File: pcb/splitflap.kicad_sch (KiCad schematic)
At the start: 62 parts, among them J1 Motor A, J10 Hall C, J11 Hall-D, J12 Conn_01x03, J13 Conn_01x03, J14 Conn_01x03, J15 Conn_01x03, J2 Motor B, J3 Motor C, J4 Motor D, J6 Conn_01x03, J7 Barrel_Jack_Switch, J8 Hall A, J9 Hall B, SW1 A, SW2 B, SW3 IO0, SW4 RST, U1 ULN2003, U12 LM2596S-5, U2 ULN2003, U3 ESP32-DevKitC, U4 ULN2003, U5 AH1815-W-7, U6 AH1815-W-7, U7 AH1815-W-7, U8 AH1815-W-7, U9 AH1815-W-7

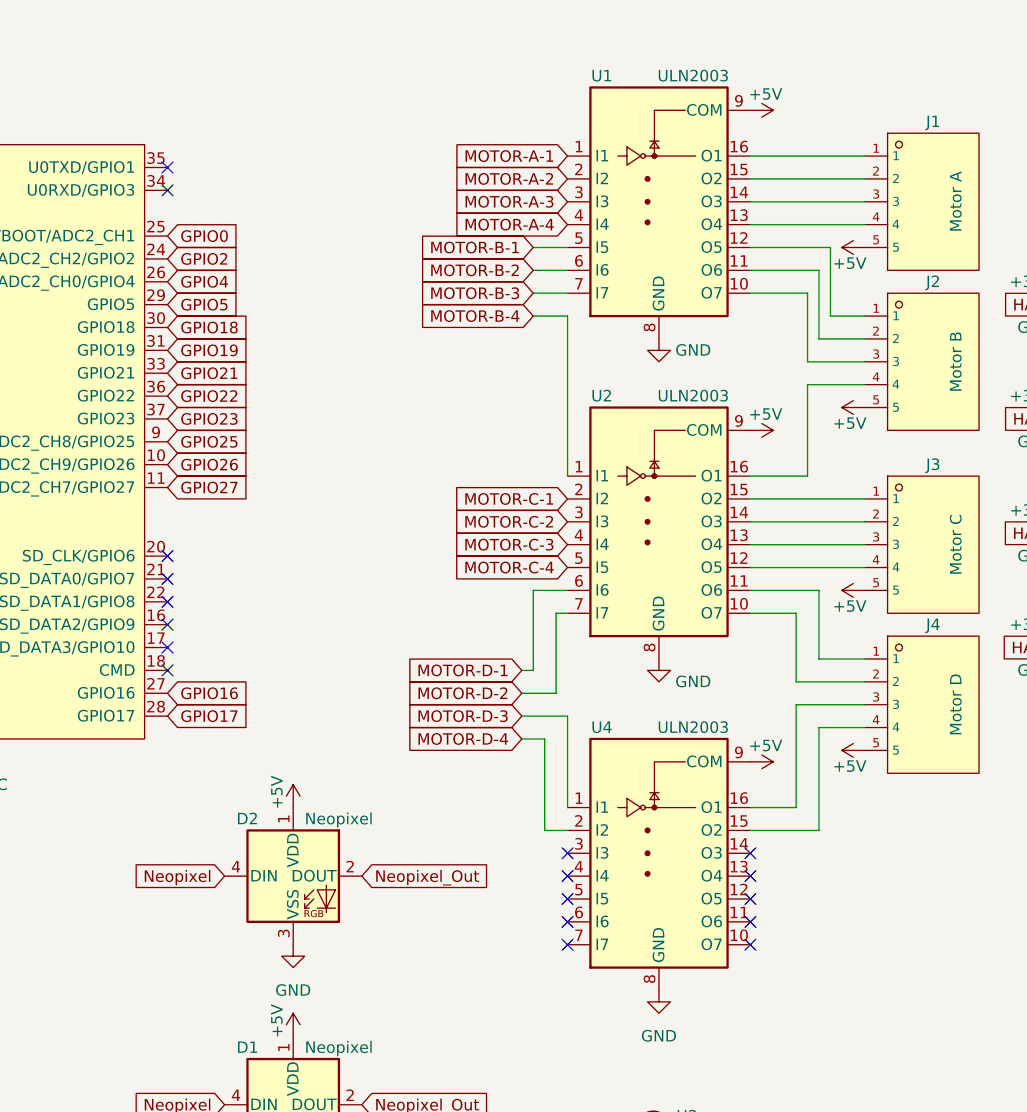
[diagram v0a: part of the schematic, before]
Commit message: Rework 1
Per EE.SO answer https://electronics.stackexchange.com/a/740530/10810
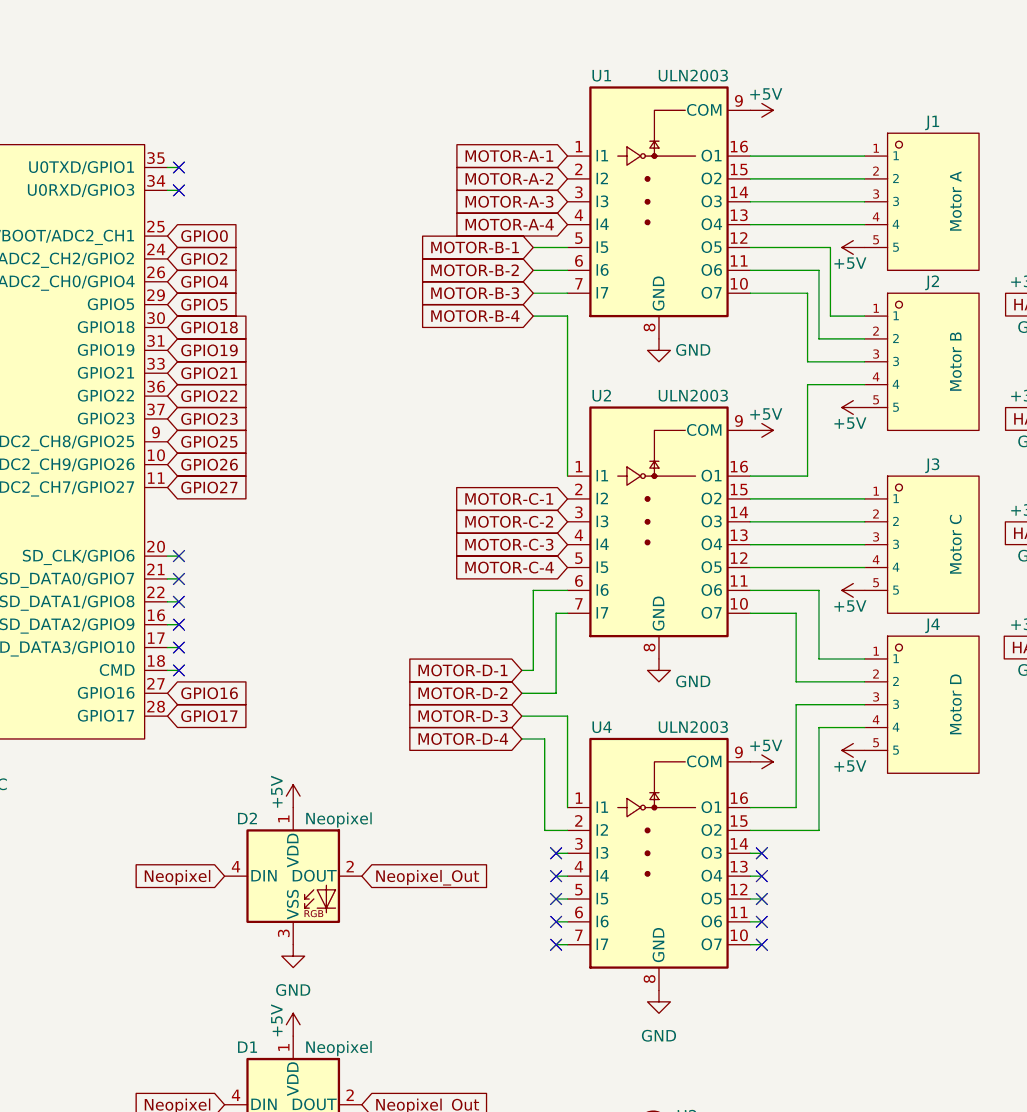
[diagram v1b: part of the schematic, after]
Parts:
- D3: footprint Diode_THT:D_DO-201_P12.70mm_Horizontal -> Diode_THT:D_DO-201_P15.24mm_Horizontal
- TP3: Label1 (none) -> SDA; Label2 (none) -> IO12
- TP4: Label1 (none) -> SCL; Label2 (none) -> IO14
- U1, U2, U4: footprint jlc_footprints:SOIC-16_L9.9-W3.9-P1.27-LS6.0-BL -> Package_SO:SOIC-16_3.9x9.9mm_P1.27mm

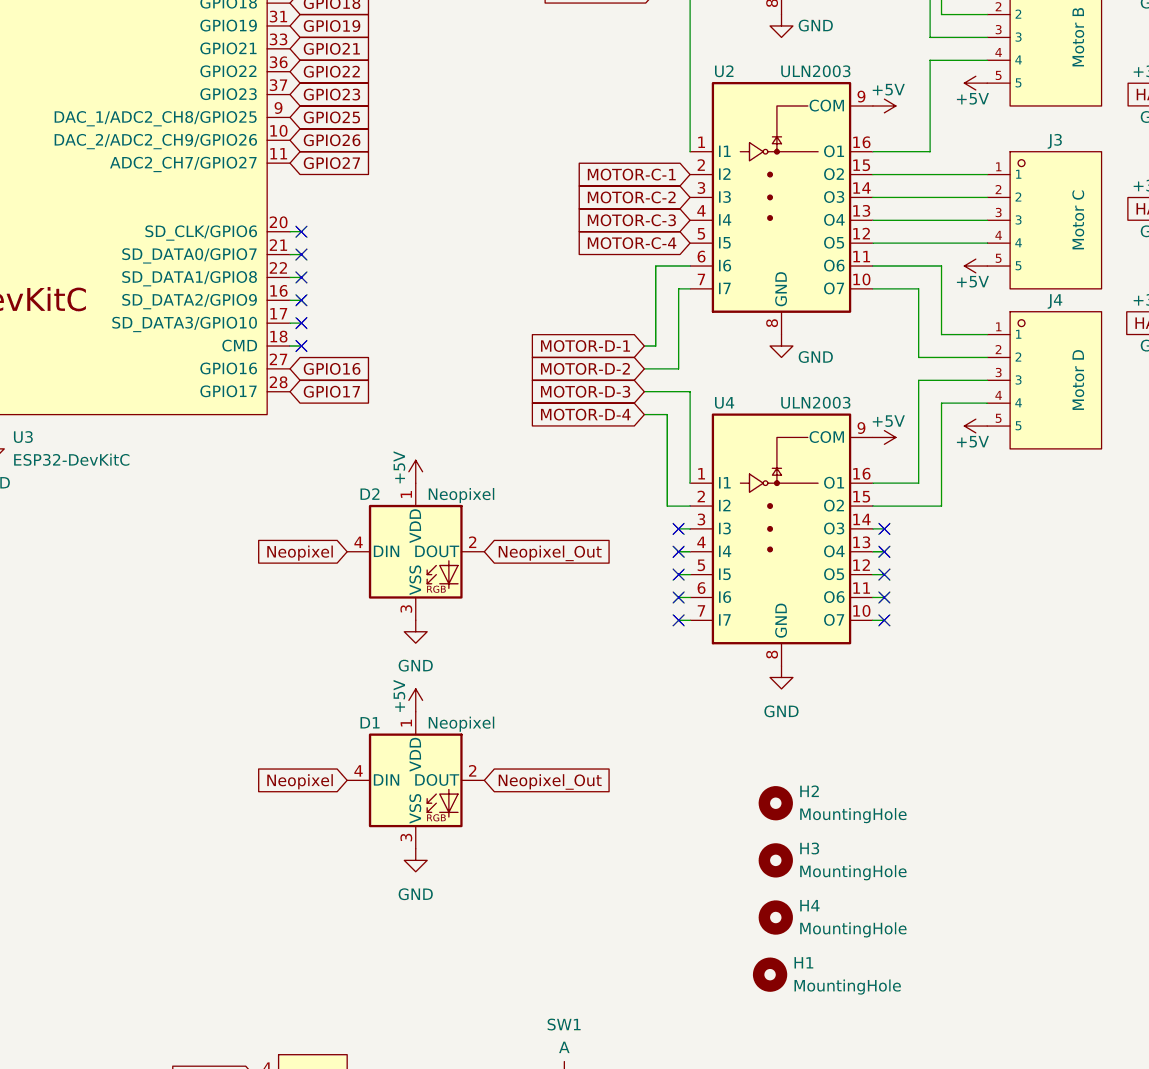
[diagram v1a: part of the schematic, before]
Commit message: Rework 3
Now the signal flow is the recommended way: inputs far away from power outputs. The Hall sensor connectors have been moved to the front of the PCB.
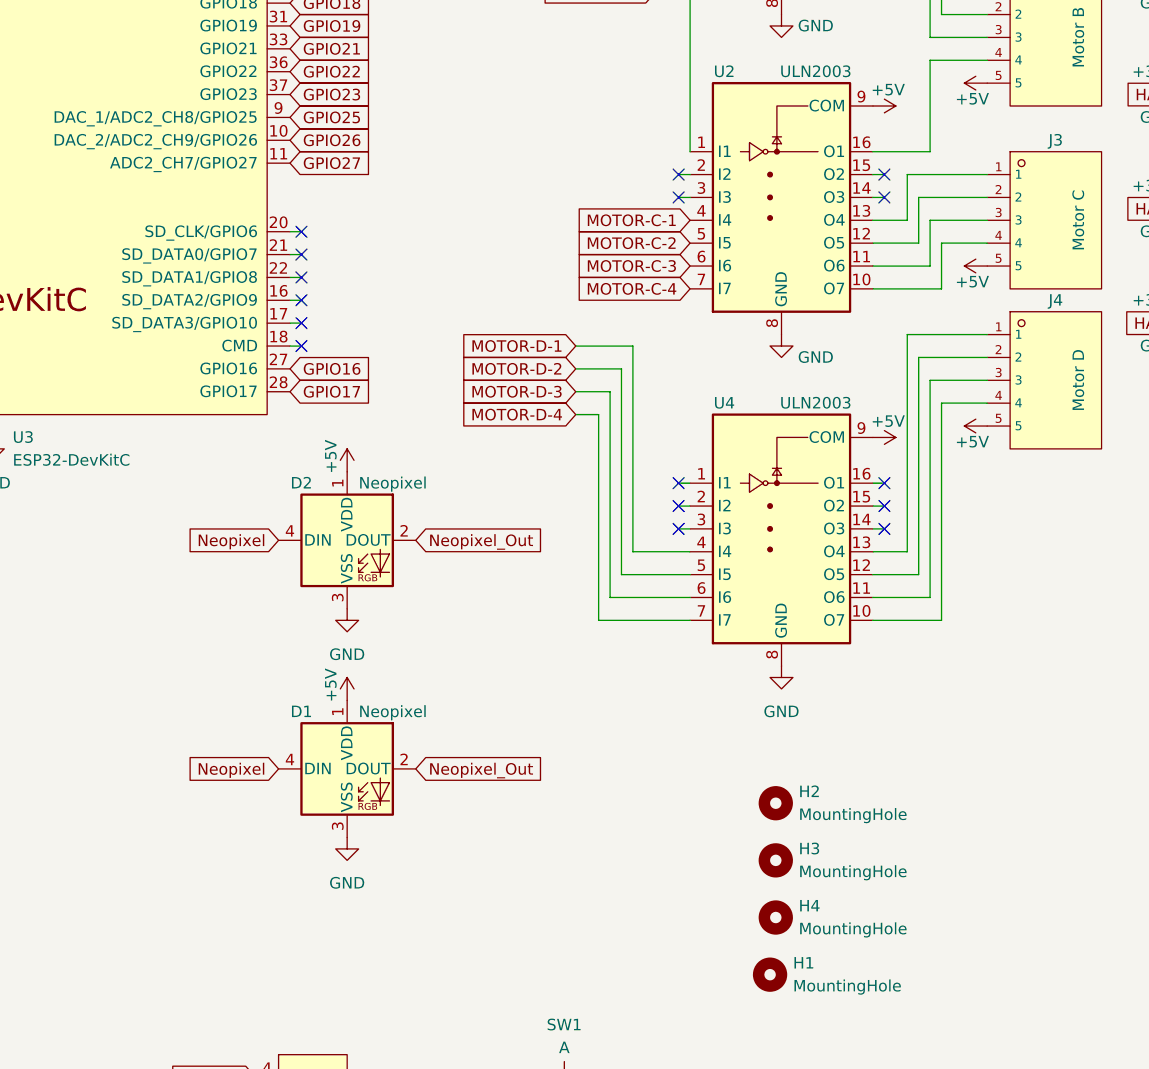
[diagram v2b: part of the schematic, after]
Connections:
- net GPIO15: now also U2.6 (I6); no longer U2.4 (I4)
- net GPIO2: now also U2.5 (I5); no longer U2.3 (I3)
- net GPIO25: now also U4.5 (I5); no longer U2.7 (I7)
- net GPIO26: now also U4.6 (I6); no longer U4.1 (I1)
- net GPIO27: now also U4.7 (I7); no longer U4.2 (I2)
- net GPIO32: now also U2.7 (I7); no longer U2.5 (I5)
- net GPIO33: now also U4.4 (I4); no longer U2.6 (I6)
- net GPIO4: now also U2.4 (I4); no longer U2.2 (I2)
- net at U2.10 (O7): now also J3.4; no longer J4.2
- net at U2.11 (O6): now also J3.3; no longer J4.1
- net at U2.12 (O5): now also J3.2; no longer J3.4
- net at U2.13 (O4): now also J3.1; no longer J3.3
- net at U2.14 (O3): no longer J3.2
- net at U2.15 (O2): no longer J3.1
- net at J4.3: now also U4.11 (O6); no longer U4.16 (O1)
- net at J4.4: now also U4.10 (O7); no longer U4.15 (O2)
- net at U4.12 (O5): now also J4.2
- net at U4.13 (O4): now also J4.1
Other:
- moved on the sheet: D1, D2

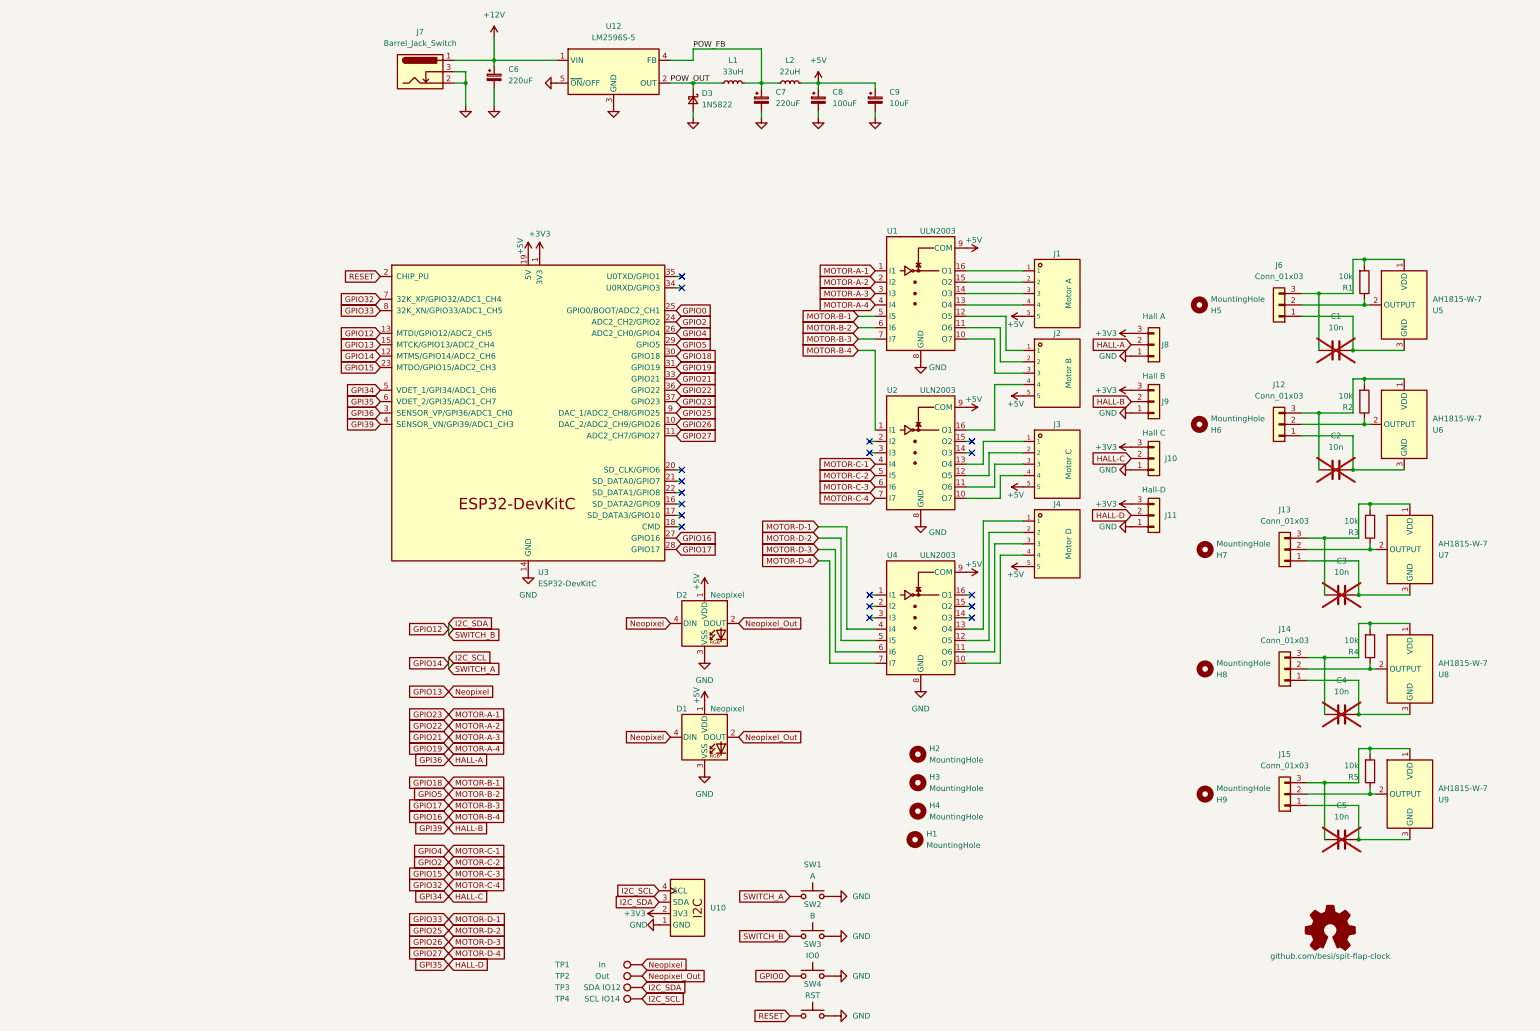
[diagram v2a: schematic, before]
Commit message: Rework 5
The schematic was separated into two sheets, and made easier to follow.

The Neopixels were connected in parallel. They should be in series.

The I2C mezzanine board was centered relative to the ESP module.
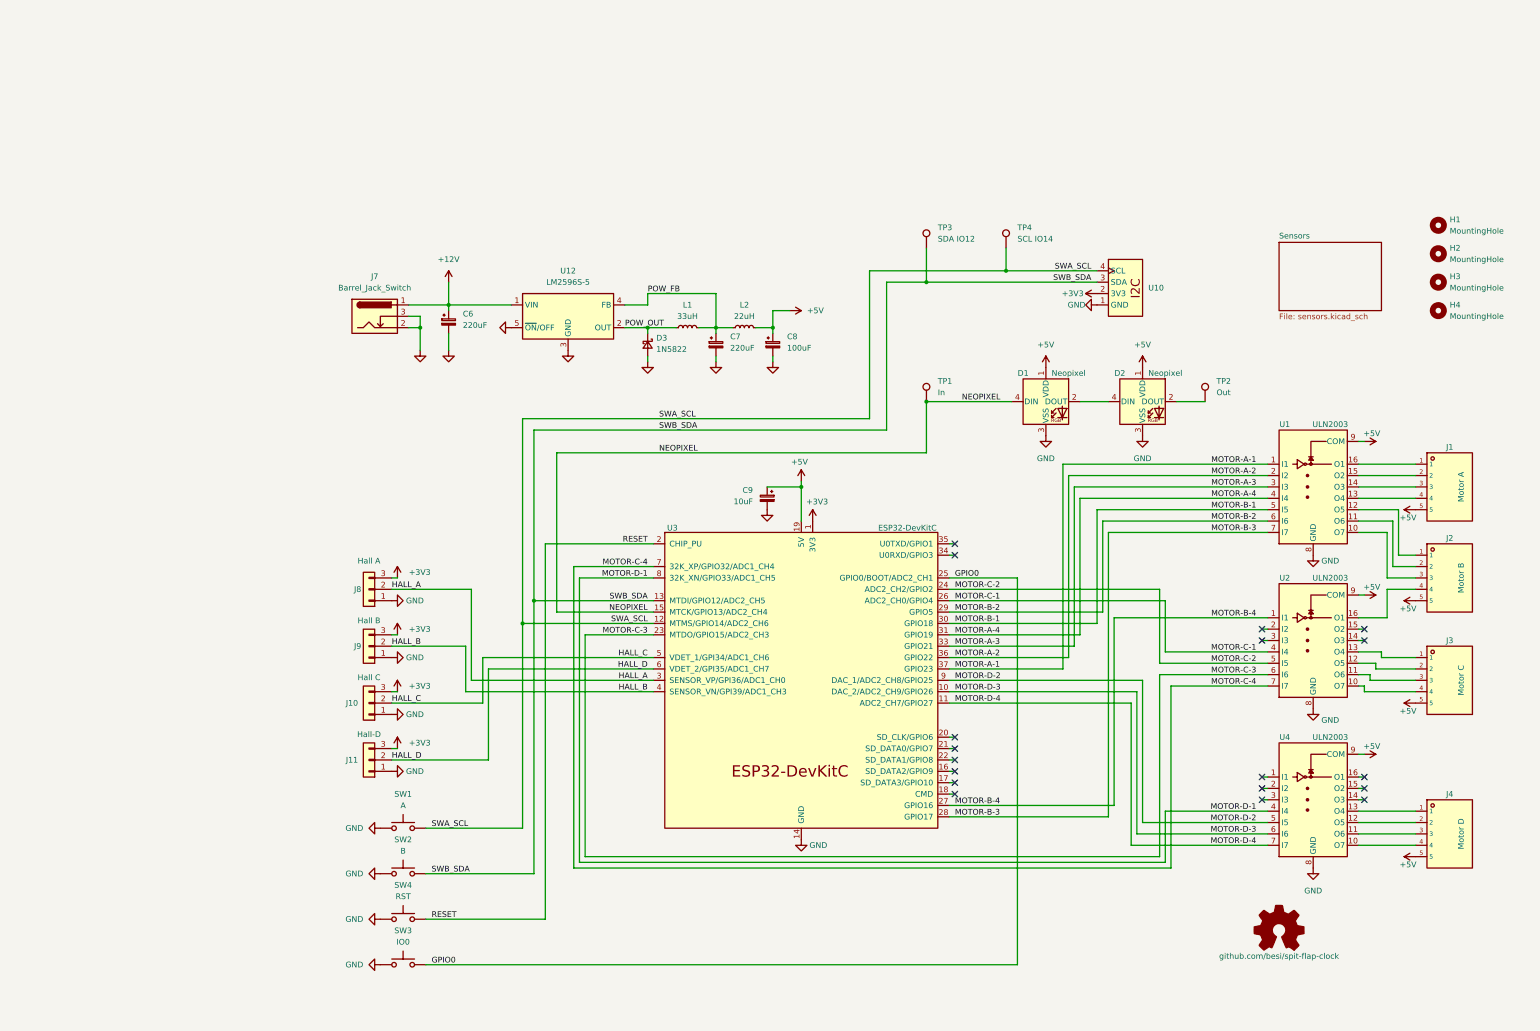
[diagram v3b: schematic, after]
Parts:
- removed C1, C2, C3, C4, C5: 10n, symbol Device:C
- removed H5, H6, H7, H8, H9: MountingHole, MountingHole:MountingHole_3.2mm_M3, symbol Mechanical:MountingHole
- removed J12, J13, J14, J15, J6: Conn_01x03, Connector_PinHeader_2.54mm:PinHeader_1x03_P2.54mm_Vertical, symbol Connector_Generic:Conn_01x03
- removed R1, R2, R3, R4, R5: 10k, Resistor_SMD:R_0805_2012Metric_Pad1.20x1.40mm_HandSolder, symbol Device:R
- removed U5, U6, U7, U8, U9: AH1815-W-7, Package_TO_SOT_SMD:SC-59_Handsoldering, symbol Sensor_Magnetic:AH1806-W
- OSHW1: now left out of the parts list
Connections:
- net GPI34 renamed HALL_C
- net GPI35 renamed HALL_D
- net GPI36 renamed HALL_A
- net GPI39 renamed HALL_B
- net GPIO12 renamed SWB_SDA
- net GPIO13 renamed NEOPIXEL
- net NEOPIXEL: no longer D2.4 (DIN)
- net GPIO14 renamed SWA_SCL
- net GPIO15 renamed MOTOR-C-3
- net GPIO16 renamed MOTOR-B-4
- net GPIO17 renamed MOTOR-B-3
- net GPIO18 renamed MOTOR-B-1
- net GPIO19 renamed MOTOR-A-4
- net GPIO2 renamed MOTOR-C-2
- net GPIO21 renamed MOTOR-A-3
- net GPIO22 renamed MOTOR-A-2
- net GPIO23 renamed MOTOR-A-1
- net GPIO25 renamed MOTOR-D-2
- net GPIO26 renamed MOTOR-D-3
- net GPIO27 renamed MOTOR-D-4
- net GPIO32 renamed MOTOR-C-4
- net GPIO33 renamed MOTOR-D-1
- net GPIO4 renamed MOTOR-C-1
- net GPIO5 renamed MOTOR-B-2
- net Neopixel_Out: no longer names the net of D2.2 (DOUT), TP2.1
- net Neopixel_Out: no longer D1.2 (DOUT)
- new net: D1.2 (DOUT), D2.4 (DIN)
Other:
- added sheet Sensors (sensors.kicad_sch)
- moved on the sheet: C6, C7, C8, C9, D1, D2, D3, H1, H2, H3, H4, J1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
